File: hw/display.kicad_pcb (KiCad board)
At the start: 2 copper layers, 87.3 x 60.3 mm, 62 parts, among them J1 AMPSEAL_8_POS_776275-1, J2 ARM_JTAG_SWD_HEADER_10_PINSMD, J3 HEADER_USART_2_SMD, J4 HEADER_MOLEX_52207-0433, J5 HEADER_MOLEX_54104-4031, U1 MCP2551_SOIC8, U2 ALLIANCE_AS4C4M16SA_TSOP_II, U3 WINDBOND_W25Q32FV_SOIC8_W, U4 LPC1785FBD208_551QFP50, U6 MOSFET-N_2N7002W, X1 XTAL_7A-20.000MAAJ-T, X2 XTAL_ABS25-32.768KHZ-T, X3 BUZZER_PKM13EPYH4002-B0

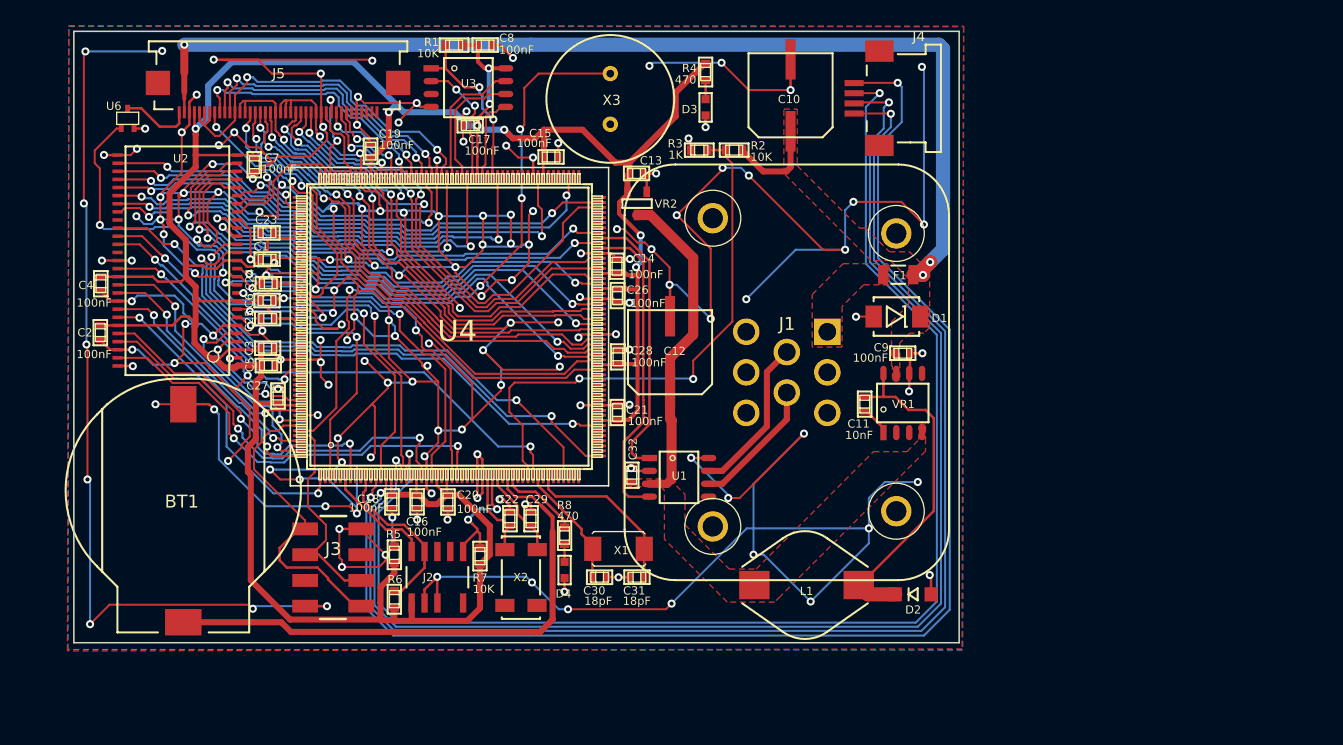
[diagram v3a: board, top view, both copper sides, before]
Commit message: starting to design hw 5.0, with variable current source for LCD backlight
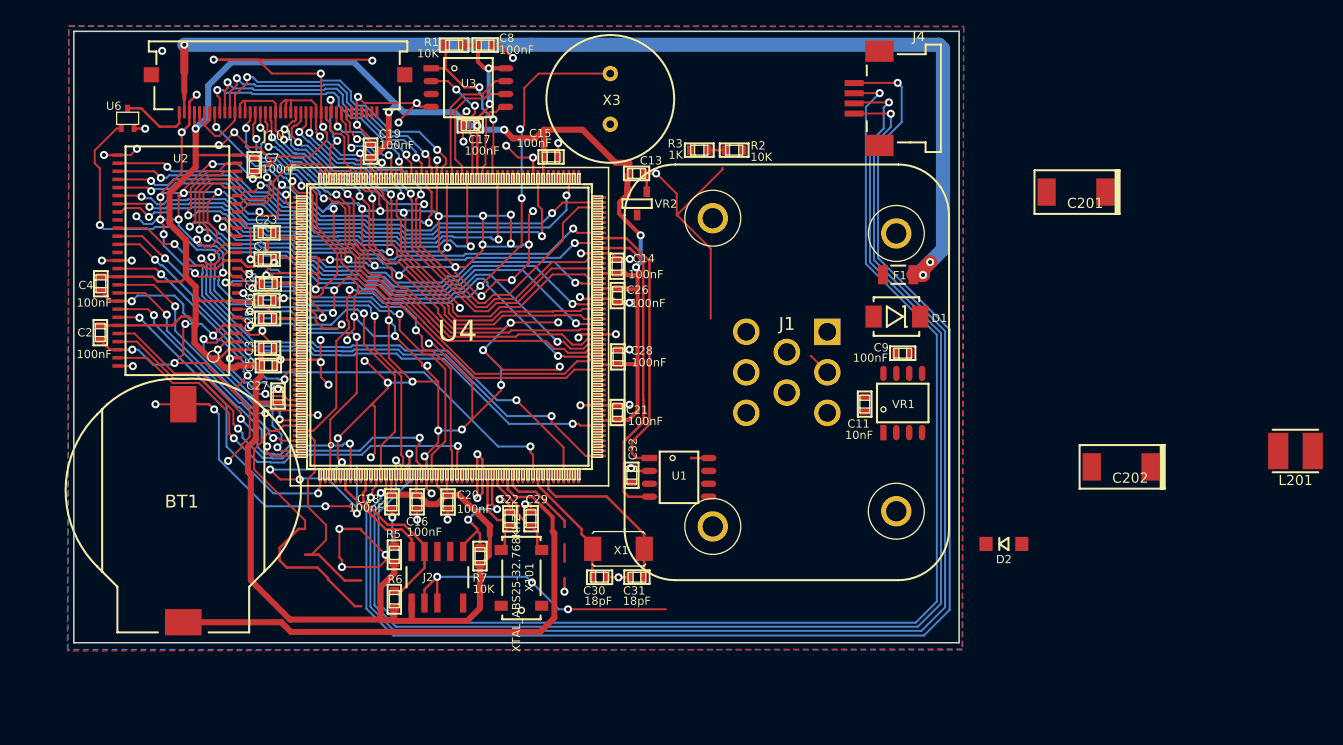
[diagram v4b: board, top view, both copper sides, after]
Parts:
- removed C10, C12: CAP_EEE-FK1H470P, usevolt:CAP_EEE-FK1H470P
- removed D3, D4: WL-SMCW-150060BS75000-B, wurth_LEDS:Wuerth_Elektronik_LEDs_rev15b-0603
- removed J3: HEADER_USART_2_SMD, usevolt:HEADER_4_2_SMD
- removed J5: HEADER_MOLEX_54104-4031, usevolt:HEADER_MOLEX_54104-4031
- removed L1: INDUCTOR_SDR1005-101KL, usevolt:INDUCTOR_BOURNS_10X13X5MM
- removed R4, R8: 470, multicomp:Multicomp-RESC1608X60N
- removed X2: XTAL_ABS25-32.768KHZ-T, usevolt:XTAL_32.768KHZ-T
- added C201: T491D226K035AT, kemet:7343, F.Cu at (186.6, 72.8)
- added C202: T491D226K035AT, kemet:7343, F.Cu at (191.1, 99.8)
- added J101: HEADER_MOLEX_54104-4031, usevolt:HEADER_MOLEX_54104-4031, F.Cu at (107.9, 62.4)
- added L201: IND_744045210, usevolt:IND_744045210, F.Cu at (208.2, 98.3)
- added X101: XTAL_ABS25-32.768KHZ-T, usevolt:XTAL_32.768KHZ-T, F.Cu at (131.9, 110.8)
- moved D2 10.2 mm to (179.5, 107.5)
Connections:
- J1 pad P$3: (no net) -> Net-(J1-PadP$3)
- J1 pad P$6: (no net) -> Net-(J1-PadP$6)
- J1 pad P$7: (no net) -> Net-(J1-PadP$7)
- J1 pad P$8: (no net) -> Net-(J1-PadP$8)
- J2 pad P$6: (no net) -> Net-(J2-PadP$6)
- J2 pad P$7: (no net) -> Net-(J2-PadP$7)
- J2 pad P$8: (no net) -> Net-(J2-PadP$8)
- U1 pad P$5: (no net) -> Net-(U1-PadP$5)
- U2 pad P$36: (no net) -> Net-(U2-PadP$36)
- U2 pad P$40: (no net) -> Net-(U2-PadP$40)
- U3 pad P$3: (no net) -> Net-(U3-PadP$3)
- U4 pad 100: (no net) -> Net-(U4-Pad100)
- U4 pad 101: (no net) -> Net-(U4-Pad101)
- U4 pad 104: (no net) -> Net-(U4-Pad104)
- U4 pad 105: (no net) -> Net-(U4-Pad105)
- U4 pad 106: (no net) -> /lpc1785_sheet/LCD_VD18
- U4 pad 108: (no net) -> Net-(U4-Pad108)
- U4 pad 109: (no net) -> Net-(U4-Pad109)
- U4 pad 11: (no net) -> Net-(U4-Pad11)
- U4 pad 110: (no net) -> Net-(U4-Pad110)
- U4 pad 111: (no net) -> Net-(U4-Pad111)
- U4 pad 115: (no net) -> Net-(U4-Pad115)
- U4 pad 116: (no net) -> Net-(U4-Pad116)
- U4 pad 117: (no net) -> Net-(U4-Pad117)
- U4 pad 118: (no net) -> Net-(U4-Pad118)
- U4 pad 119: (no net) -> Net-(U4-Pad119)
- U4 pad 120: (no net) -> Net-(U4-Pad120)
- U4 pad 123: (no net) -> Net-(U4-Pad123)
- U4 pad 129: (no net) -> Net-(U4-Pad129)
- U4 pad 137: (no net) -> Net-(U4-Pad137)
- U4 pad 139: (no net) -> Net-(U4-Pad139)
- U4 pad 141: (no net) -> Net-(U4-Pad141)
- U4 pad 143: (no net) -> Net-(U4-Pad143)
- U4 pad 147: (no net) -> Net-(U4-Pad147)
- U4 pad 149: (no net) -> Net-(U4-Pad149)
- U4 pad 151: (no net) -> Net-(U4-Pad151)
- U4 pad 152: (no net) -> Net-(U4-Pad152)
- U4 pad 153: (no net) -> Net-(U4-Pad153)
- U4 pad 156: (no net) -> Net-(U4-Pad156)
- U4 pad 157: (no net) -> Net-(U4-Pad157)
- U4 pad 158: (no net) -> /lpc1785_sheet/LCD_VD17
- U4 pad 160: (no net) -> /lpc1785_sheet/LCD_VD16
- U4 pad 161: (no net) -> Net-(U4-Pad161)
- U4 pad 162: (no net) -> /lpc1785_sheet/LCD_VD9
- U4 pad 163: (no net) -> Net-(U4-Pad163)
- U4 pad 164: (no net) -> /lpc1785_sheet/LCD_VD8
- U4 pad 166: (no net) -> /lpc1785_sheet/LCD_VD1
- U4 pad 167: (no net) -> Net-(U4-Pad167)
- U4 pad 168: (no net) -> /lpc1785_sheet/LCD_VD0
- U4 pad 170: (no net) -> /lpc1785_sheet/LCD_VD2
- U4 pad 171: (no net) -> Net-(U4-Pad171)
- U4 pad 173: (no net) -> Net-(U4-Pad173)
- U4 pad 175: (no net) -> Net-(U4-Pad175)
- U4 pad 178: (no net) -> Net-(U4-Pad178)
- U4 pad 180: (no net) -> Net-(U4-Pad180)
- U4 pad 182: (no net) -> Net-(U4-Pad182)
- U4 pad 183: (no net) -> Net-(U4-Pad183)
- U4 pad 184: (no net) -> Net-(U4-Pad184)
- U4 pad 185: (no net) -> Net-(U4-Pad185)
- U4 pad 186: (no net) -> Net-(U4-Pad186)
- U4 pad 187: (no net) -> Net-(U4-Pad187)
- U4 pad 188: (no net) -> Net-(U4-Pad188)
- U4 pad 19: (no net) -> Net-(U4-Pad19)
- U4 pad 190: (no net) -> Net-(U4-Pad190)
- U4 pad 192: (no net) -> Net-(U4-Pad192)
- U4 pad 193: (no net) -> Net-(U4-Pad193)
- U4 pad 194: (no net) -> Net-(U4-Pad194)
- U4 pad 195: (no net) -> Net-(U4-Pad195)
- U4 pad 196: (no net) -> Net-(U4-Pad196)
- U4 pad 2: (no net) -> Net-(U4-Pad2)
- U4 pad 202: /TXD -> Net-(U4-Pad202)
- U4 pad 204: /RXD -> Net-(U4-Pad204)
- U4 pad 206: (no net) -> Net-(U4-Pad206)
- U4 pad 25: (no net) -> Net-(U4-Pad25)
- U4 pad 29: (no net) -> Net-(U4-Pad29)
- U4 pad 30: (no net) -> Net-(U4-Pad30)
- U4 pad 31: (no net) -> Net-(U4-Pad31)
- U4 pad 37: (no net) -> Net-(U4-Pad37)
- U4 pad 4: (no net) -> Net-(U4-Pad4)
- U4 pad 40: (no net) -> Net-(U4-Pad40)
- U4 pad 41: (no net) -> Net-(U4-Pad41)
- U4 pad 45: (no net) -> Net-(U4-Pad45)
- U4 pad 47: (no net) -> Net-(U4-Pad47)
- U4 pad 48: (no net) -> Net-(U4-Pad48)
- U4 pad 5: (no net) -> Net-(U4-Pad5)
- U4 pad 50: (no net) -> Net-(U4-Pad50)
- U4 pad 51: (no net) -> Net-(U4-Pad51)
- U4 pad 52: (no net) -> Net-(U4-Pad52)
- U4 pad 54: (no net) -> Net-(U4-Pad54)
- U4 pad 55: (no net) -> Net-(U4-Pad55)
- U4 pad 56: (no net) -> Net-(U4-Pad56)
- U4 pad 57: (no net) -> Net-(U4-Pad57)
- U4 pad 58: (no net) -> Net-(U4-Pad58)
- U4 pad 61: (no net) -> Net-(U4-Pad61)
- U4 pad 62: (no net) -> Net-(U4-Pad62)
- U4 pad 64: (no net) -> Net-(U4-Pad64)
- U4 pad 65: (no net) -> Net-(U4-Pad65)
- U4 pad 66: (no net) -> Net-(U4-Pad66)
- U4 pad 67: (no net) -> Net-(U4-Pad67)
- U4 pad 68: (no net) -> Net-(U4-Pad68)
- U4 pad 69: (no net) -> Net-(U4-Pad69)
- U4 pad 8: (no net) -> Net-(U4-Pad8)
- U4 pad 81: (no net) -> Net-(U4-Pad81)
- U4 pad 85: (no net) -> Net-(U4-Pad85)
- U4 pad 9: (no net) -> Net-(U4-Pad9)
- U4 pad 91: (no net) -> Net-(U4-Pad91)
- U4 pad 98: (no net) -> Net-(U4-Pad98)
- U4 pad 99: (no net) -> Net-(U4-Pad99)
- VR1 pad P$2: (no net) -> Net-(VR1-PadP$2)
- VR1 pad P$3: (no net) -> Net-(VR1-PadP$3)
- VR1 pad P$5: (no net) -> Net-(VR1-PadP$5)
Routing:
- net GND: track 968.6 -> 702.9 mm, vias 170 -> 132
- net /lpc1785_sheet/VDD_SENSE: track 54.2 -> 1.76 mm, vias 2 -> 0
- net Net-(C11-Pad2): track 34.3 -> 0.76 mm
- net +5V: track 32.5 -> 0.00 mm
- net Net-(U4-Pad202): track 0.00 -> 30.1 mm
- net /TXD: track 30.1 -> 0.00 mm
- net Net-(U4-Pad204): track 0.00 -> 21.7 mm
- net /RXD: track 21.7 -> 0.00 mm
- net /CANH: track 15.7 -> 0.00 mm
- net /CANL: track 13.0 -> 0.00 mm
- net +3V3: track 320.9 -> 308.0 mm
- net VDD: track 115.8 -> 106.5 mm
- net (no net): track 0.00 -> 3.11 mm, vias 0 -> 2
- net Net-(C11-Pad1): track 2.97 -> 0.00 mm
- net Net-(D3-Pad2): track 1.84 -> 0.00 mm
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- removed copper zone on F.Cu, net +5V
- removed copper zone on F.Cu, net /pwr_supply_sheet/VIN
- removed copper zone on F.Cu, net VDD

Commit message: still implementing treeview, not ready
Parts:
- removed R2: 10K, multicomp:Multicomp-RESC1608X60N
- removed R3: 1K, multicomp:Multicomp-RESC1608X60N
- removed U6: MOSFET-N_2N7002W, usevolt:SOT323
- added C101: 100nF, kemet:0603, F.Cu at (148.9, 65.5)
- added D101: DIODE_RS07J-GS18, usevolt:DO219AB, F.Cu at (149.1, 61.4)
- added F201: FUSE_MC36211_350MA, usevolt:FUSE_MC36211, F.Cu at (162.0, 80.3)
- added L101: INDUCTOR_SDR1005-101KL, usevolt:INDUCTOR_BOURNS_10X13X5MM, F.Cu at (157.6, 65.1)
- added R101: R_0.33OHM, usevolt:0603, F.Cu at (151.8, 68.1)
- added R301: 10K, multicomp:0603, F.Cu at (121.2, 66.7)
- added U101: MOSFET-N_2N7002W, usevolt:SOT323, F.Cu at (144.6, 68.2)
- added U102: AL8805W5-7_LED_DRIVER, usevolt:SOT-25, F.Cu at (148.8, 68.2)
- moved L201 38.9 mm to (169.3, 99.0)
- moved C201 26.1 mm to (160.8, 77.2), turned to 180 degrees
- moved C202 24.4 mm to (169.1, 110.5), turned to 180 degrees
- moved C32 19.3 mm to (146.0, 81.6)
- moved U1 19.3 mm to (150.6, 81.8)
- moved D2 16.0 mm to (163.9, 104.0), turned to 90 degrees
- moved C29 11.8 mm to (123.9, 112.7), turned to 0 degrees
- moved R7 9.36 mm to (118.5, 108.5)
- moved R6 9.30 mm to (110.1, 112.6)
- moved J2 9.30 mm to (111.8, 111.7)
- moved R5 9.30 mm to (110.1, 108.2)
- moved X101 8.05 mm to (124.0, 109.5), turned to 180 degrees
- moved F1 7.40 mm to (162.0, 83.1)
- moved C22 6.91 mm to (124.0, 106.4), turned to 0 degrees
- moved C30 6.81 mm to (134.0, 106.9)
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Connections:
- J101 pad 2: VDD -> /BCKL+
- U4 pad 177: /BACKLIGHT -> Net-(U4-Pad177)
- U4 pad 203: /lpc1785_sheet/BUZZER -> Net-(U4-Pad203)
- U4 pad 42: /lpc1785_sheet/VDD_SENSE -> Net-(U4-Pad42)
- U4 pad 56: Net-(U4-Pad56) -> /lpc1785_sheet/BUZZER
- U4 pad 58: Net-(U4-Pad58) -> /BACKLIGHT
- X3 pad 1: /lpc1785_sheet/BUZZER -> Net-(U101-PadR)
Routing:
- net GND: track 702.9 -> 907.0 mm, vias 132 -> 147
- net +5V: track 0.00 -> 78.4 mm
- net /BCKL+: track 0.00 -> 74.7 mm, vias 0 -> 2
- net /BCKL-: track 7.07 -> 67.0 mm, vias 0 -> 2
- net VDD: track 106.5 -> 54.4 mm, vias 3 -> 0
- net Net-(U4-Pad202): track 30.1 -> 0.00 mm
- net /pwr_supply_sheet/VLCD: track 0.00 -> 27.1 mm
- net /lpc1785_sheet/BUZZER: track 61.4 -> 36.6 mm, vias 4 -> 2
- net Net-(U4-Pad204): track 21.7 -> 0.00 mm
- net /lpc1785_sheet/CAN_RXD: track 31.2 -> 11.9 mm
- net Net-(C11-Pad2): track 0.76 -> 19.2 mm
- net /lpc1785_sheet/CAN_TXD: track 27.5 -> 9.31 mm
- net Net-(L101-PadP$1): track 0.00 -> 12.5 mm
- net /CANL: track 0.00 -> 12.2 mm
- net /BACKLIGHT: track 43.0 -> 32.3 mm
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
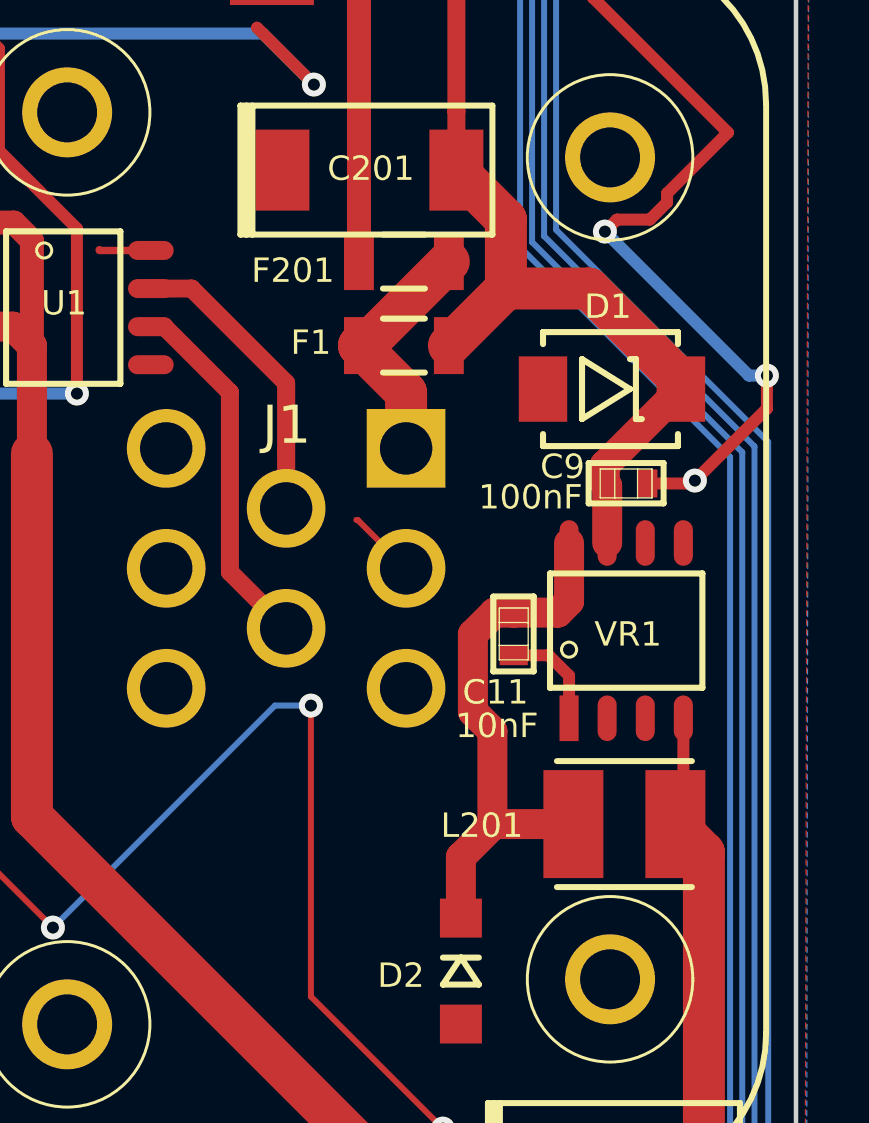
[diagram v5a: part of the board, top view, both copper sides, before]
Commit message: version control bug: pwr_supply_sheet now has fuse for LCD as in hw 1.5.0
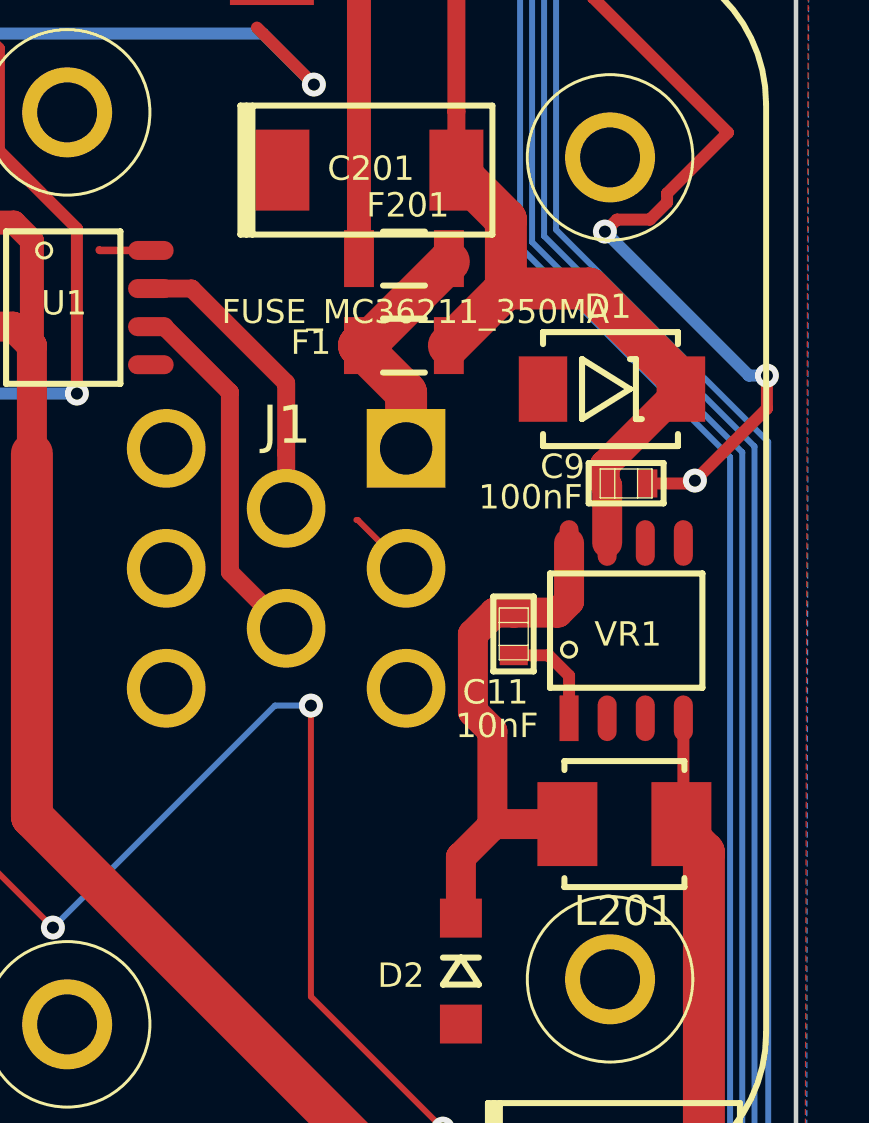
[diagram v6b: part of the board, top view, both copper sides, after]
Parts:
- moved F201 0.10 mm to (162.0, 80.2)
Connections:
- J1 pad P$3: Net-(J1-PadP$3) -> (no net)
- J1 pad P$6: Net-(J1-PadP$6) -> (no net)
- J1 pad P$7: Net-(J1-PadP$7) -> (no net)
- J1 pad P$8: Net-(J1-PadP$8) -> (no net)
- J101 pad 35: Net-(J101-Pad35) -> (no net)
- J101 pad 37: Net-(J101-Pad37) -> (no net)
- J101 pad 38: Net-(J101-Pad38) -> (no net)
- J101 pad 39: Net-(J101-Pad39) -> (no net)
- J101 pad 40: Net-(J101-Pad40) -> (no net)
- J2 pad P$6: Net-(J2-PadP$6) -> (no net)
- J2 pad P$7: Net-(J2-PadP$7) -> (no net)
- J2 pad P$8: Net-(J2-PadP$8) -> (no net)
- U1 pad P$5: Net-(U1-PadP$5) -> (no net)
- U2 pad P$36: Net-(U2-PadP$36) -> (no net)
- U2 pad P$40: Net-(U2-PadP$40) -> (no net)
- U3 pad P$3: Net-(U3-PadP$3) -> (no net)
- U4 pad 100: Net-(U4-Pad100) -> (no net)
- U4 pad 101: Net-(U4-Pad101) -> (no net)
- U4 pad 104: Net-(U4-Pad104) -> (no net)
- U4 pad 105: Net-(U4-Pad105) -> (no net)
- U4 pad 106: /lpc1785_sheet/LCD_VD18 -> (no net)
- U4 pad 108: Net-(U4-Pad108) -> (no net)
- U4 pad 109: Net-(U4-Pad109) -> (no net)
- U4 pad 11: Net-(U4-Pad11) -> (no net)
- U4 pad 110: Net-(U4-Pad110) -> (no net)
- U4 pad 111: Net-(U4-Pad111) -> (no net)
- U4 pad 115: Net-(U4-Pad115) -> (no net)
- U4 pad 116: Net-(U4-Pad116) -> (no net)
- U4 pad 117: Net-(U4-Pad117) -> (no net)
- U4 pad 118: Net-(U4-Pad118) -> (no net)
- U4 pad 119: Net-(U4-Pad119) -> (no net)
- U4 pad 120: Net-(U4-Pad120) -> (no net)
- U4 pad 123: Net-(U4-Pad123) -> (no net)
- U4 pad 129: Net-(U4-Pad129) -> (no net)
- U4 pad 137: Net-(U4-Pad137) -> (no net)
- U4 pad 139: Net-(U4-Pad139) -> (no net)
- U4 pad 141: Net-(U4-Pad141) -> (no net)
- U4 pad 143: Net-(U4-Pad143) -> (no net)
- U4 pad 147: Net-(U4-Pad147) -> (no net)
- U4 pad 149: Net-(U4-Pad149) -> (no net)
- U4 pad 151: Net-(U4-Pad151) -> (no net)
- U4 pad 152: Net-(U4-Pad152) -> (no net)
- U4 pad 153: Net-(U4-Pad153) -> (no net)
- U4 pad 156: Net-(U4-Pad156) -> (no net)
- U4 pad 157: Net-(U4-Pad157) -> (no net)
- U4 pad 158: /lpc1785_sheet/LCD_VD17 -> (no net)
- U4 pad 160: /lpc1785_sheet/LCD_VD16 -> (no net)
- U4 pad 161: Net-(U4-Pad161) -> (no net)
- U4 pad 162: /lpc1785_sheet/LCD_VD9 -> (no net)
- U4 pad 163: Net-(U4-Pad163) -> (no net)
- U4 pad 164: /lpc1785_sheet/LCD_VD8 -> (no net)
- U4 pad 166: /lpc1785_sheet/LCD_VD1 -> (no net)
- U4 pad 167: Net-(U4-Pad167) -> (no net)
- U4 pad 168: /lpc1785_sheet/LCD_VD0 -> (no net)
- U4 pad 170: /lpc1785_sheet/LCD_VD2 -> (no net)
- U4 pad 171: Net-(U4-Pad171) -> (no net)
- U4 pad 173: Net-(U4-Pad173) -> (no net)
- U4 pad 175: Net-(U4-Pad175) -> (no net)
- U4 pad 177: Net-(U4-Pad177) -> (no net)
- U4 pad 178: Net-(U4-Pad178) -> (no net)
- U4 pad 180: Net-(U4-Pad180) -> (no net)
- U4 pad 182: Net-(U4-Pad182) -> (no net)
- U4 pad 183: Net-(U4-Pad183) -> (no net)
- U4 pad 184: Net-(U4-Pad184) -> (no net)
- U4 pad 185: Net-(U4-Pad185) -> (no net)
- U4 pad 186: Net-(U4-Pad186) -> (no net)
- U4 pad 187: Net-(U4-Pad187) -> (no net)
- U4 pad 188: Net-(U4-Pad188) -> (no net)
- U4 pad 19: Net-(U4-Pad19) -> (no net)
- U4 pad 190: Net-(U4-Pad190) -> (no net)
- U4 pad 192: Net-(U4-Pad192) -> (no net)
- U4 pad 193: Net-(U4-Pad193) -> (no net)
- U4 pad 194: Net-(U4-Pad194) -> (no net)
- U4 pad 195: Net-(U4-Pad195) -> (no net)
- U4 pad 196: Net-(U4-Pad196) -> (no net)
- U4 pad 2: Net-(U4-Pad2) -> (no net)
- U4 pad 202: Net-(U4-Pad202) -> (no net)
- U4 pad 203: Net-(U4-Pad203) -> (no net)
- U4 pad 204: Net-(U4-Pad204) -> (no net)
- U4 pad 206: Net-(U4-Pad206) -> (no net)
- U4 pad 25: Net-(U4-Pad25) -> (no net)
- U4 pad 29: Net-(U4-Pad29) -> (no net)
- U4 pad 30: Net-(U4-Pad30) -> (no net)
- U4 pad 31: Net-(U4-Pad31) -> (no net)
- U4 pad 37: Net-(U4-Pad37) -> (no net)
- U4 pad 39: Net-(U4-Pad39) -> (no net)
- U4 pad 4: Net-(U4-Pad4) -> (no net)
- U4 pad 40: Net-(U4-Pad40) -> (no net)
- U4 pad 41: Net-(U4-Pad41) -> (no net)
- U4 pad 42: Net-(U4-Pad42) -> (no net)
- U4 pad 45: Net-(U4-Pad45) -> (no net)
- U4 pad 47: Net-(U4-Pad47) -> (no net)
- U4 pad 48: Net-(U4-Pad48) -> (no net)
- U4 pad 5: Net-(U4-Pad5) -> (no net)
- U4 pad 50: Net-(U4-Pad50) -> (no net)
- U4 pad 51: Net-(U4-Pad51) -> (no net)
- U4 pad 52: Net-(U4-Pad52) -> (no net)
- U4 pad 54: Net-(U4-Pad54) -> (no net)
- U4 pad 55: Net-(U4-Pad55) -> (no net)
- U4 pad 57: Net-(U4-Pad57) -> (no net)
- U4 pad 61: Net-(U4-Pad61) -> (no net)
- U4 pad 62: Net-(U4-Pad62) -> (no net)
- U4 pad 64: Net-(U4-Pad64) -> (no net)
- U4 pad 65: Net-(U4-Pad65) -> (no net)
- U4 pad 66: Net-(U4-Pad66) -> (no net)
- U4 pad 67: Net-(U4-Pad67) -> (no net)
- U4 pad 68: Net-(U4-Pad68) -> (no net)
- U4 pad 69: Net-(U4-Pad69) -> (no net)
- U4 pad 8: Net-(U4-Pad8) -> (no net)
- U4 pad 81: Net-(U4-Pad81) -> (no net)
- U4 pad 85: Net-(U4-Pad85) -> (no net)
- U4 pad 9: Net-(U4-Pad9) -> (no net)
- U4 pad 91: Net-(U4-Pad91) -> (no net)
- U4 pad 98: Net-(U4-Pad98) -> (no net)
- U4 pad 99: Net-(U4-Pad99) -> (no net)
- VR1 pad P$2: Net-(VR1-PadP$2) -> (no net)
- VR1 pad P$3: Net-(VR1-PadP$3) -> (no net)
- VR1 pad P$5: Net-(VR1-PadP$5) -> (no net)
